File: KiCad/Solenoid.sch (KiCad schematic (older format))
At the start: 4 parts

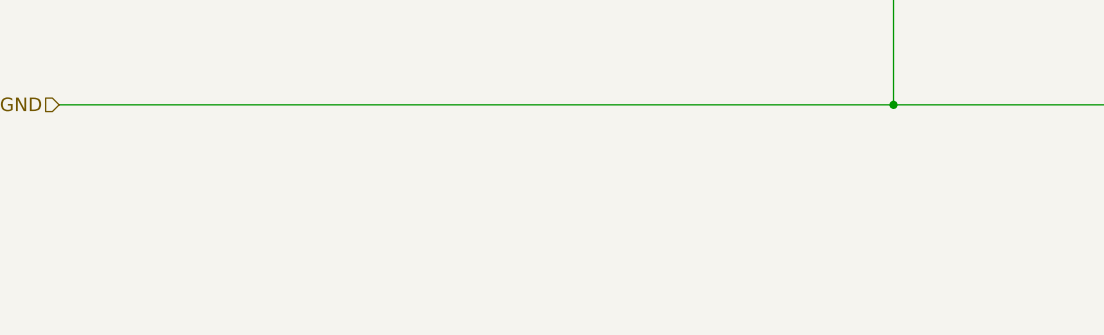
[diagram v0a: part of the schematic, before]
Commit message: add Programming Arduino for temp connection to program KCX_BT_EMITTER
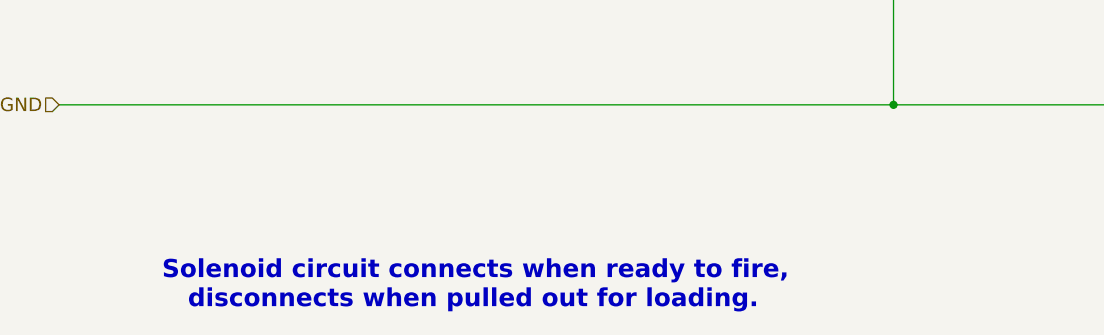
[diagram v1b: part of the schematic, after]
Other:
- note added: "Solenoid circuit connects when ready to fire,\n disconnects when pulled out for loading."
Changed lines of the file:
@@
 $Descr A4 11693 8268
 encoding utf-8
-Sheet 2 3
+Sheet 2 4
 Title "Detail: Solenoid Driver"
-Date "2020-08-26"
+Date "2020-09-07"
 Rev ""
 Comp ""
@@
 Text Notes 10850 1650 2    157  ~ 31
 Derived from https://cdn-shop-adafruit.com/product-files/412/solenoid_driver.pdf
+Text Notes 2950 6400 0    79   ~ 16
+Solenoid circuit connects when ready to fire,\n   disconnects when pulled out for loading.
 $EndSCHEMATC

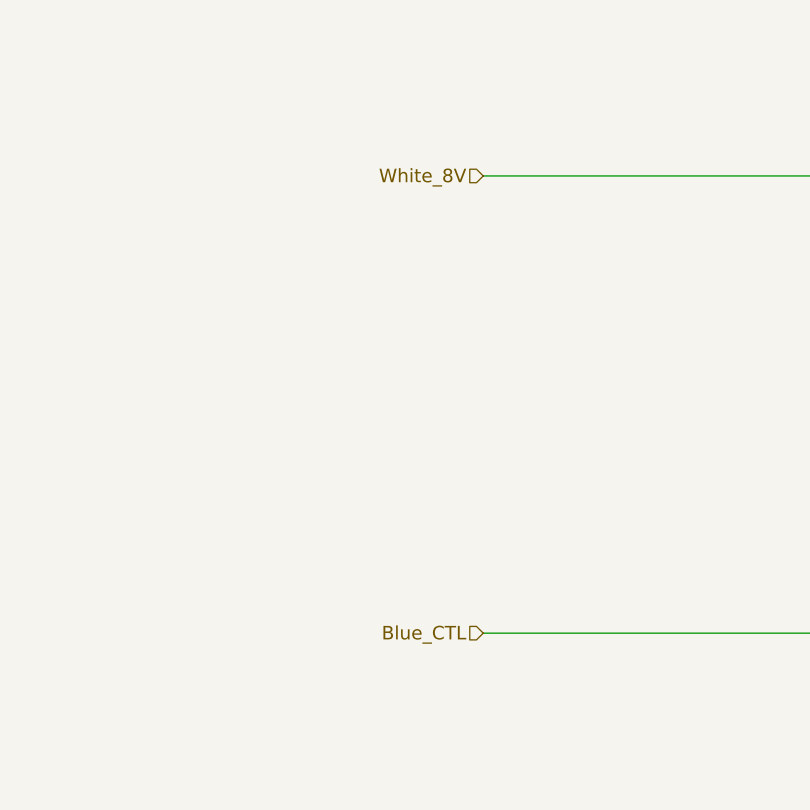
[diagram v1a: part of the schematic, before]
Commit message: use new color scheme for USB connector
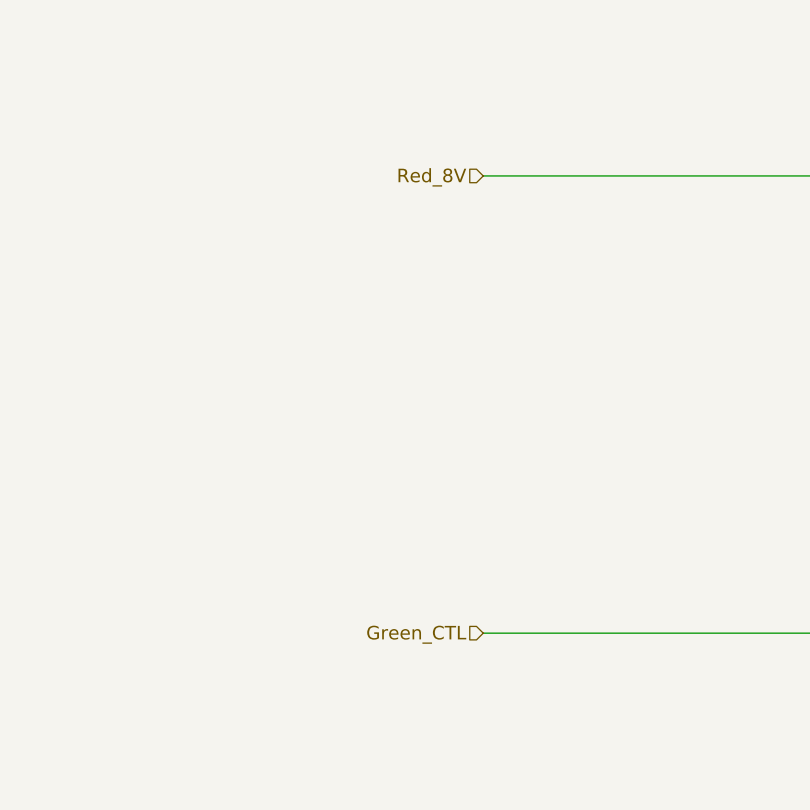
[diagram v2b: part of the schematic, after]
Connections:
- net Blue_CTL renamed Green_CTL
- net White_8V renamed Red_8V
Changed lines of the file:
@@
 Sheet 2 4
 Title "Detail: Solenoid Driver"
-Date "2020-09-07"
+Date "2020-09-12"
 Rev ""
 Comp ""
@@
 	6150 3800 6150 4300
 Text HLabel 2500 2500 0    59   Input ~ 0
-White_8V
+Red_8V
 Text HLabel 2500 4500 0    59   Input ~ 0
-Blue_CTL
+Green_CTL
 Text HLabel 2500 5500 0    59   Input ~ 0
 Black_GND
